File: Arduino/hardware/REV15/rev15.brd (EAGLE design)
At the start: 50 x 50 mm, 20 parts, among them IC2 ATMEGA168-AU, Q1 32768Hz

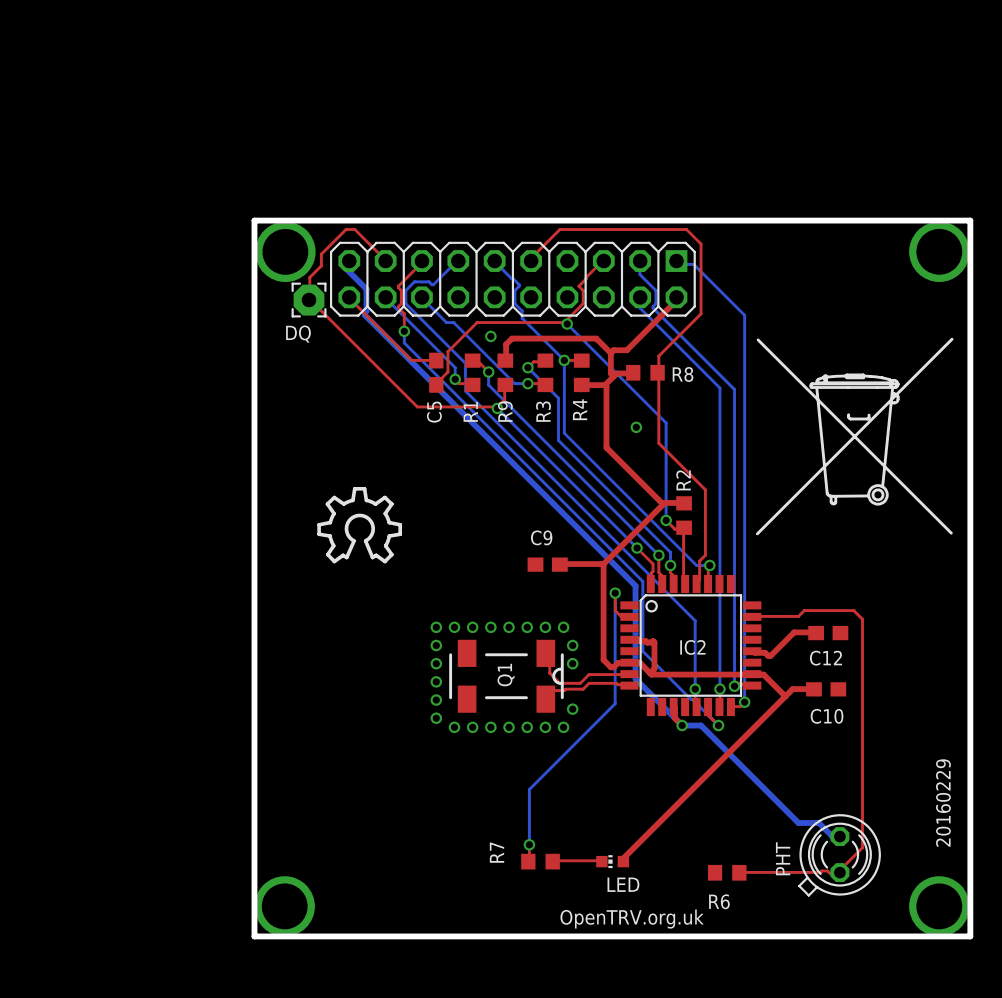
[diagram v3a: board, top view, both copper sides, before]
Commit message: rev15-18 changed as per Deniz suggeastions
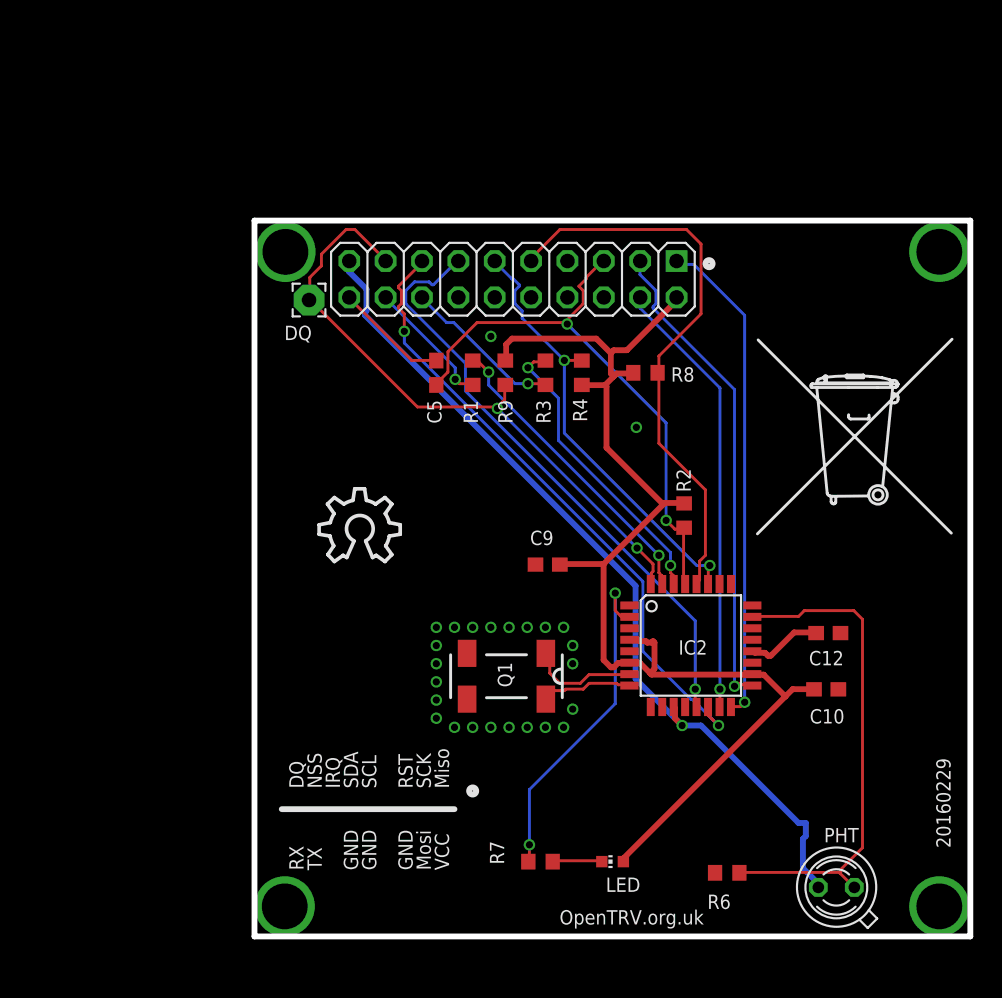
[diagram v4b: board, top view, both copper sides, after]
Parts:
- moved PHT 2.30 mm to (40.6, 3.42), turned to 135 degrees
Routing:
- net IO_POWER_UP: track 57.9 -> 60.2 mm
- net LDR: track 33.7 -> 35.0 mm
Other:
- board text added: "GND"
- board text added: "IRQ"
- board text added: "Miso"
- board text added: "Mosi"
- board text added: "NSS"
- board text added: "RST"
- board text added: "RX"
- board text added: "SCK"
- board text added: "SCL"
- board text added: "SDA"
- board text added: "TX"
- board text added: "VCC"
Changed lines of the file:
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@@
 <wire x1="50" y1="0" x2="0" y2="0" width="0.4064" layer="20"/>
 <text x="2.085" y="41.655" size="1" layer="25" font="vector">DQ</text>
+<text x="3.43" y="10.34" size="1" layer="25" rot="R90">DQ</text>
+<text x="7.24" y="10.34" size="1" layer="25" rot="R90">SDA</text>
+<text x="13.59" y="10.34" size="1" layer="25" rot="R90">Miso</text>
+<text x="13.59" y="4.625" size="1" layer="25" rot="R90">VCC</text>
+<text x="12.32" y="10.34" size="1" layer="25" rot="R90">SCK</text>
+<text x="12.32" y="4.625" size="1" layer="25" rot="R90">Mosi</text>
+<text x="11.05" y="10.34" size="1" layer="25" rot="R90">RST</text>
+<text x="11.05" y="4.625" size="1" layer="25" rot="R90">GND</text>
+<text x="5.97" y="10.34" size="1" layer="25" rot="R90">IRQ</text>
+<text x="4.7" y="10.34" size="1" layer="25" rot="R90">NSS</text>
+<text x="3.43" y="4.625" size="1" layer="25" rot="R90">RX</text>
+<text x="8.51" y="10.34" size="1" layer="25" rot="R90">SCL</text>
+<text x="4.7" y="4.625" size="1" layer="25" rot="R90">TX</text>
+<wire x1="13.97" y1="8.89" x2="1.905" y2="8.89" width="0.4064" layer="25"/>
+<text x="8.51" y="4.625" size="1" layer="25" rot="R90">GND</text>
+<text x="7.24" y="4.625" size="1" layer="25" rot="R90">GND</text>
+<circle x="15.24" y="10.16" radius="0.25" width="0.4064" layer="25"/>
+<circle x="31.75" y="46.99" radius="0.25" width="0.4064" layer="25"/>
 </plain>
 <attributes>
@@
 <attribute name="NAME" x="33.274" y="2.921" size="1" layer="25" font="vector" rot="R180"/>
 </element>
-<element name="PHT" library="opto-trans-siemens" package="BPX65" value="BPX65" x="40.89" y="5.715" smashed="yes" rot="R45">
-<attribute name="MF" value="" x="45.380125" y="1.224871875" size="1.778" layer="27" rot="R45" display="off"/>
-<attribute name="OC_FARNELL" value="327451" x="45.380125" y="1.224871875" size="1.778" layer="27" rot="R45" display="off"/>
-<attribute name="OC_NEWARK" value="06WX2764" x="45.380125" y="1.224871875" size="1.778" layer="27" rot="R45" display="off"/>
-<attribute name="MPN" value="BPX65." x="45.380125" y="1.224871875" size="1.778" layer="27" rot="R45" display="off"/>
-<attribute name="NAME" x="37.420059375" y="4.1500625" size="1" layer="25" font="vector" rot="R90"/>
+<element name="PHT" library="opto-trans-siemens" package="BPX65" value="BPX65" x="40.64" y="3.425" smashed="yes" rot="R135">
+<attribute name="MF" value="" x="45.130128125" y="7.915125" size="1.778" layer="27" rot="R135" display="off"/>
+<attribute name="OC_FARNELL" value="327451" x="45.130128125" y="7.915125" size="1.778" layer="27" rot="R135" display="off"/>
+<attribute name="OC_NEWARK" value="06WX2764" x="45.130128125" y="7.915125" size="1.778" layer="27" rot="R135" display="off"/>
+<attribute name="MPN" value="BPX65." x="45.130128125" y="7.915125" size="1.778" layer="27" rot="R135" display="off"/>
+<attribute name="NAME" x="42.2049375" y="7.575059375" size="1" layer="25" font="vector" rot="R180"/>
 </element>
 <element name="R9" library="resistor" package="R0603" value="4.7K" x="17.52" y="39.37" smashed="yes" rot="R90">
@@
 <contactref element="PHT" pad="A"/>
 <contactref element="IC2" pad="23"/>
-<wire x1="39.5224" y1="4.4704" x2="33.9344" y2="4.4704" width="0.2032" layer="1"/>
-<wire x1="39.624" y1="4.572" x2="39.5224" y2="4.4704" width="0.2032" layer="1"/>
-<wire x1="40.0304" y1="4.572" x2="39.624" y2="4.572" width="0.2032" layer="1"/>
-<wire x1="40.2336" y1="4.3688" x2="40.0304" y2="4.572" width="0.2032" layer="1"/>
-<wire x1="40.8432" y1="4.3688" x2="40.2336" y2="4.3688" width="0.2032" layer="1"/>
 <wire x1="33.9344" y1="4.4704" x2="33.87" y2="4.445" width="0.2032" layer="1"/>
-<wire x1="40.8432" y1="4.3688" x2="40.89" y2="4.4577625" width="0.2032" layer="1"/>
 <wire x1="37.9984" y1="22.352" x2="34.8488" y2="22.352" width="0.2032" layer="1"/>
 <wire x1="38.4048" y1="22.7584" x2="37.9984" y2="22.352" width="0.2032" layer="1"/>
@@
 <wire x1="42.4688" y1="22.1488" x2="41.8592" y2="22.7584" width="0.2032" layer="1"/>
 <wire x1="42.4688" y1="6.1976" x2="42.4688" y2="22.1488" width="0.2032" layer="1"/>
-<wire x1="40.9448" y1="4.6736" x2="42.4688" y2="6.1976" width="0.2032" layer="1"/>
-<wire x1="40.9448" y1="4.4704" x2="40.9448" y2="4.6736" width="0.2032" layer="1"/>
 <wire x1="34.8488" y1="22.352" x2="34.7726" y2="22.32" width="0.2032" layer="1"/>
-<wire x1="40.9448" y1="4.4704" x2="40.89" y2="4.4577625" width="0.2032" layer="1"/>
+<wire x1="40.8432" y1="4.4704" x2="34.036" y2="4.4704" width="0.2032" layer="1"/>
+<wire x1="41.8592" y1="3.4544" x2="40.894" y2="4.4196" width="0.2032" layer="1"/>
+<wire x1="40.894" y1="4.4196" x2="40.8432" y2="4.4704" width="0.2032" layer="1"/>
+<wire x1="34.036" y1="4.4704" x2="33.87" y2="4.445" width="0.2032" layer="1"/>
+<wire x1="41.8592" y1="3.4544" x2="41.897234375" y2="3.425" width="0.2032" layer="1"/>
+<wire x1="40.9448" y1="4.6736" x2="40.9448" y2="4.4704" width="0.2032" layer="1"/>
+<wire x1="42.4688" y1="6.1976" x2="40.9448" y2="4.6736" width="0.2032" layer="1"/>
+<wire x1="40.9448" y1="4.4704" x2="40.894" y2="4.4196" width="0.2032" layer="1"/>
 </signal>
 <signal name="IO_POWER_UP" class="1">
@@
 <wire x1="31.1912" y1="14.732" x2="29.8704" y2="14.732" width="0.4064" layer="16"/>
 <wire x1="37.9984" y1="7.9248" x2="31.1912" y2="14.732" width="0.4064" layer="16"/>
-<wire x1="39.4208" y1="7.9248" x2="37.9984" y2="7.9248" width="0.4064" layer="16"/>
-<wire x1="40.3352" y1="7.0104" x2="39.4208" y2="7.9248" width="0.4064" layer="16"/>
-<wire x1="40.8432" y1="7.0104" x2="40.3352" y2="7.0104" width="0.4064" layer="16"/>
+<wire x1="38.5064" y1="7.9248" x2="37.9984" y2="7.9248" width="0.4064" layer="16"/>
 <wire x1="29.3624" y1="15.9512" x2="29.28" y2="16.0274" width="0.4064" layer="1"/>
-<wire x1="40.8432" y1="7.0104" x2="40.89" y2="6.972234375" width="0.4064" layer="16"/>
 <wire x1="6.604" y1="46.4312" x2="6.604" y2="47.1424" width="0.4064" layer="16"/>
 <wire x1="7.8232" y1="45.212" x2="6.604" y2="46.4312" width="0.4064" layer="16"/>
@@
 <wire x1="6.604" y1="47.1424" x2="6.62" y2="47.175" width="0.4064" layer="16"/>
 <via x="29.8704" y="14.732" extent="1-16" drill="0.5"/>
+<wire x1="39.3192" y1="3.7592" x2="39.3192" y2="3.4544" width="0.4064" layer="16"/>
+<wire x1="38.3032" y1="4.7752" x2="39.3192" y2="3.7592" width="0.4064" layer="16"/>
+<wire x1="38.3032" y1="6.8072" x2="38.3032" y2="4.7752" width="0.4064" layer="16"/>
+<wire x1="38.5064" y1="7.0104" x2="38.3032" y2="6.8072" width="0.4064" layer="16"/>
+<wire x1="38.5064" y1="7.9248" x2="38.5064" y2="7.0104" width="0.4064" layer="16"/>
+<wire x1="39.3192" y1="3.4544" x2="39.3827625" y2="3.425" width="0.4064" layer="16"/>
 </signal>
 <signal name="N$24">

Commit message: ic2_ext labels closer to connector
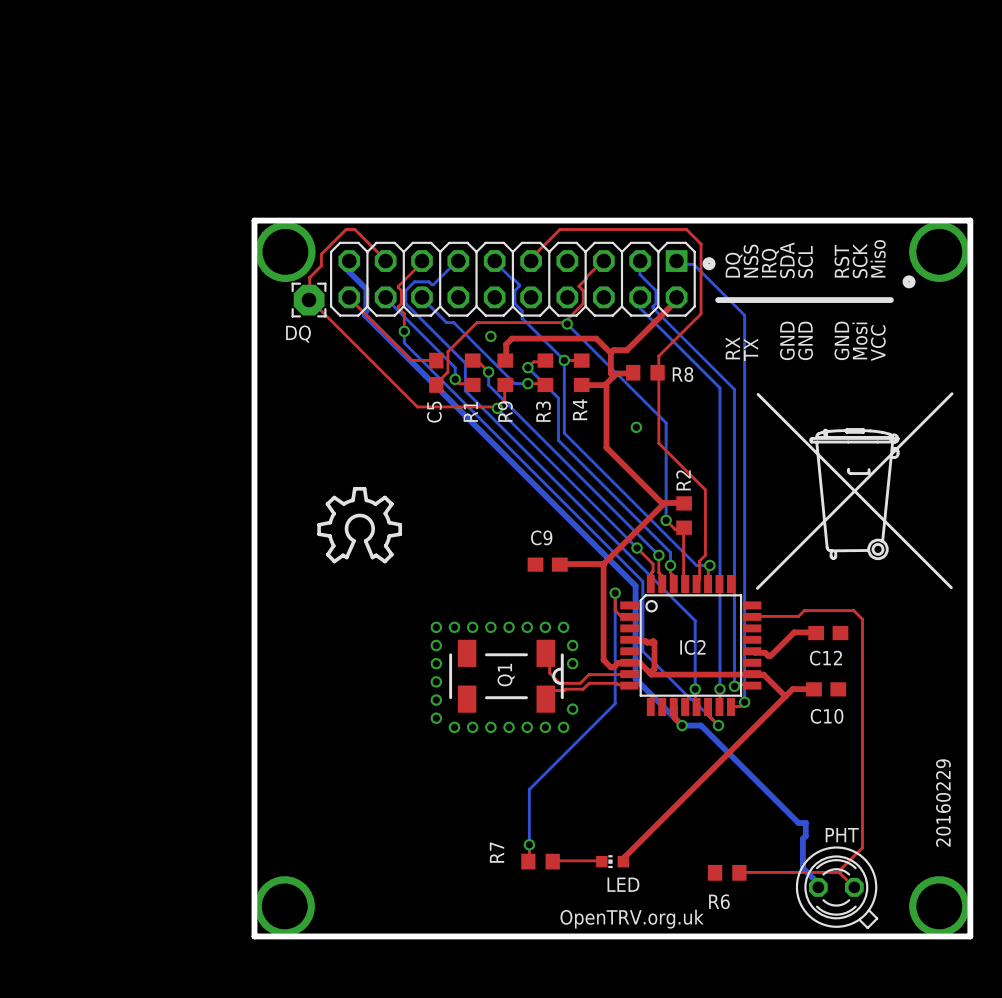
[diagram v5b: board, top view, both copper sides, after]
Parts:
- moved U$2 3.81 mm to (41.8, 28.4)
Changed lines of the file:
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@@
 <wire x1="50" y1="0" x2="0" y2="0" width="0.4064" layer="20"/>
 <text x="2.085" y="41.655" size="1" layer="25" font="vector">DQ</text>
-<text x="3.43" y="10.34" size="1" layer="25" rot="R90">DQ</text>
-<text x="7.24" y="10.34" size="1" layer="25" rot="R90">SDA</text>
-<text x="13.59" y="10.34" size="1" layer="25" rot="R90">Miso</text>
-<text x="13.59" y="4.625" size="1" layer="25" rot="R90">VCC</text>
-<text x="12.32" y="10.34" size="1" layer="25" rot="R90">SCK</text>
-<text x="12.32" y="4.625" size="1" layer="25" rot="R90">Mosi</text>
-<text x="11.05" y="10.34" size="1" layer="25" rot="R90">RST</text>
-<text x="11.05" y="4.625" size="1" layer="25" rot="R90">GND</text>
-<text x="5.97" y="10.34" size="1" layer="25" rot="R90">IRQ</text>
-<text x="4.7" y="10.34" size="1" layer="25" rot="R90">NSS</text>
-<text x="3.43" y="4.625" size="1" layer="25" rot="R90">RX</text>
-<text x="8.51" y="10.34" size="1" layer="25" rot="R90">SCL</text>
-<text x="4.7" y="4.625" size="1" layer="25" rot="R90">TX</text>
-<wire x1="13.97" y1="8.89" x2="1.905" y2="8.89" width="0.4064" layer="25"/>
-<text x="8.51" y="4.625" size="1" layer="25" rot="R90">GND</text>
-<text x="7.24" y="4.625" size="1" layer="25" rot="R90">GND</text>
-<circle x="15.24" y="10.16" radius="0.25" width="0.4064" layer="25"/>
+<text x="33.91" y="45.9" size="1" layer="25" rot="R90">DQ</text>
+<text x="37.72" y="45.9" size="1" layer="25" rot="R90">SDA</text>
+<text x="44.07" y="45.9" size="1" layer="25" rot="R90">Miso</text>
+<text x="44.07" y="40.185" size="1" layer="25" rot="R90">VCC</text>
+<text x="42.8" y="45.9" size="1" layer="25" rot="R90">SCK</text>
+<text x="42.8" y="40.185" size="1" layer="25" rot="R90">Mosi</text>
+<text x="41.53" y="45.9" size="1" layer="25" rot="R90">RST</text>
+<text x="41.53" y="40.185" size="1" layer="25" rot="R90">GND</text>
+<text x="36.45" y="45.9" size="1" layer="25" rot="R90">IRQ</text>
+<text x="35.18" y="45.9" size="1" layer="25" rot="R90">NSS</text>
+<text x="33.91" y="40.185" size="1" layer="25" rot="R90">RX</text>
+<text x="38.99" y="45.9" size="1" layer="25" rot="R90">SCL</text>
+<text x="35.18" y="40.185" size="1" layer="25" rot="R90">TX</text>
+<wire x1="44.45" y1="44.45" x2="32.385" y2="44.45" width="0.4064" layer="25"/>
+<text x="38.99" y="40.185" size="1" layer="25" rot="R90">GND</text>
+<text x="37.72" y="40.185" size="1" layer="25" rot="R90">GND</text>
+<circle x="45.72" y="45.72" radius="0.25" width="0.4064" layer="25"/>
 <circle x="31.75" y="46.99" radius="0.25" width="0.4064" layer="25"/>
 </plain>
@@
 <attribute name="NAME" x="17.440165625" y="5.0265" size="1" layer="25" font="vector" rot="R90"/>
 </element>
-<element name="U$2" library="logo" package="TONNE" value="" x="41.775" y="32.16711875"/>
+<element name="U$2" library="logo" package="TONNE" value="" x="41.775" y="28.35711875"/>
 <element name="R2" library="resistor" package="R0603" value="4.7K" x="30.006046875" y="29.3970875" smashed="yes" rot="R270">
 <attribute name="NAME" x="30.47489375" y="31.03400625" size="1" layer="25" font="vector" rot="R90"/>
